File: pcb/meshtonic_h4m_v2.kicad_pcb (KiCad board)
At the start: 6 copper layers, 71.1 x 168.4 mm, 118 parts, among them J1 GROVE-CONNECTOR-DIP_4P-2.0_, J10 Conn_01x02, J11 Conn_01x02, J12 JST_2mm_LiPo, J13 Screw_Terminal_01x02, J14 Micro_SD_Card_passive_clk, J15 H4M_2x6_MDK, J2 GROVE-CONNECTOR-DIP-90D_4P-2.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, J3 GROVE-CONNECTOR-DIP_4P-2.0_, J4 GROVE-CONNECTOR-DIP_4P-2.0_, J5 GROVE-CONNECTOR-DIP_4P-2.0_, J6 GROVE-CONNECTOR-DIP_4P-2.0_, J7 GROVE-CONNECTOR-DIP_4P-2.0_, J8 GROVE-CONNECTOR-SMD_4+2P-2.0_, J9 Conn_01x02, U1 TPS63020DSJR, U2 CN3170, U3 XIAO-S3-Plus, U4 TCA9548APWR, U5 MCP23017x-x-SS

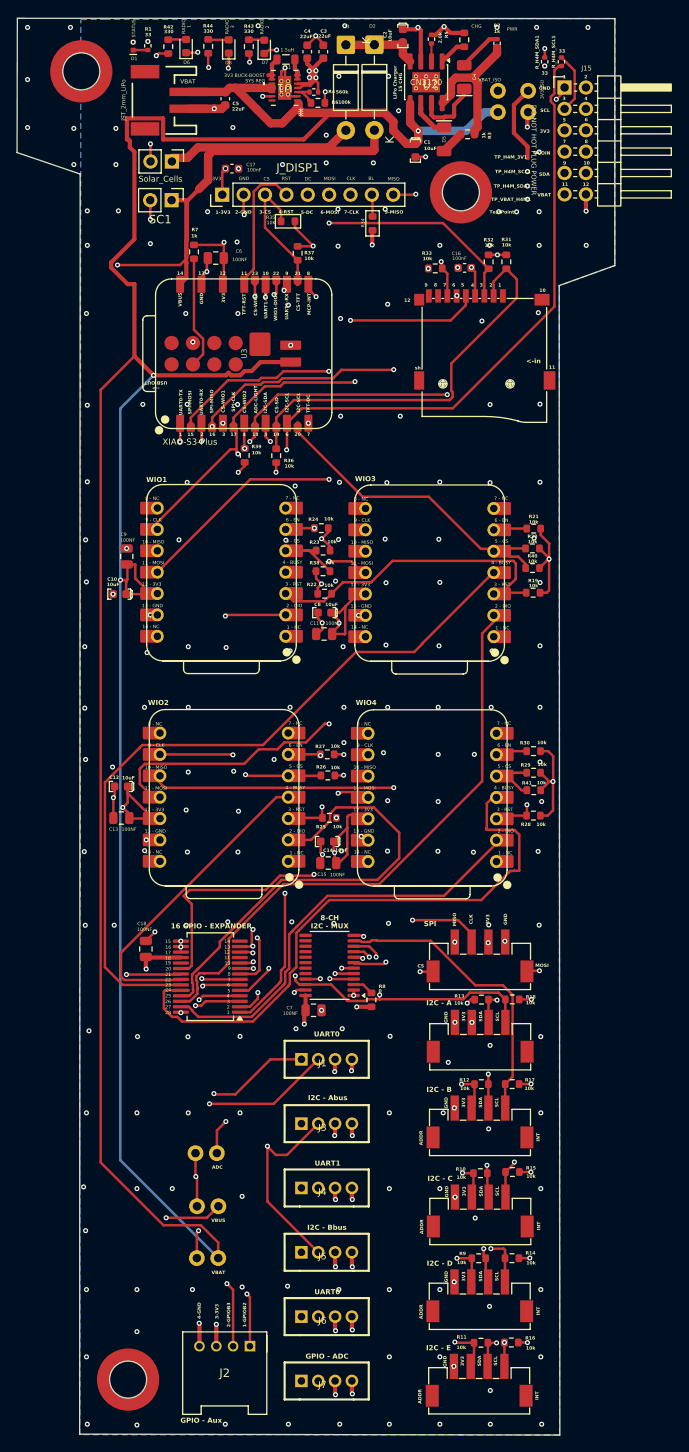
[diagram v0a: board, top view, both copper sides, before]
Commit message: solves no more direct-to-pin vias and routings
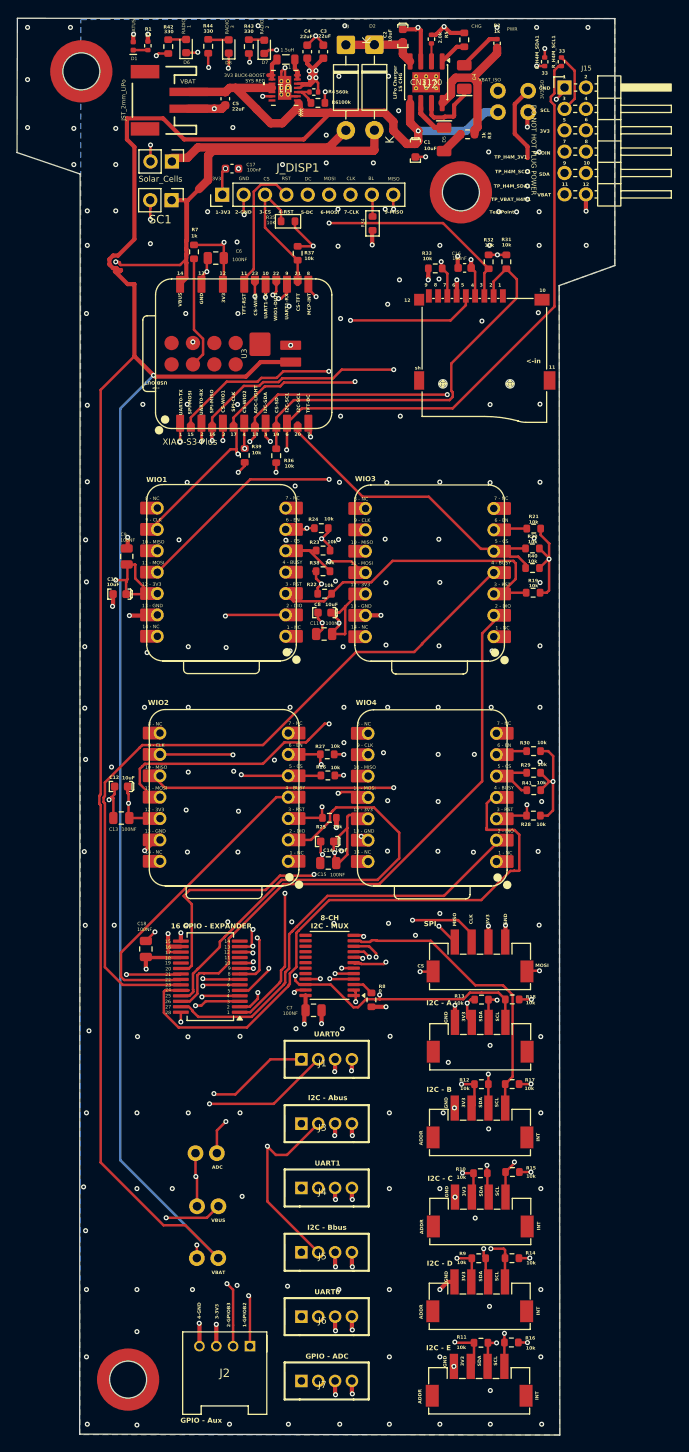
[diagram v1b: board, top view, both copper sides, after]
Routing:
- net GND: track 83.1 -> 108.9 mm, vias 228 -> 230
- net 3V3: track 192.2 -> 198.3 mm, vias 53 -> 52
- net UART1_TX: track 123.2 -> 119.7 mm
- net TFT_DC: track 27.5 -> 31.0 mm
- net SPI_MISO: track 184.0 -> 182.2 mm
- net VBUS: track 201.5 -> 202.9 mm
- net I2C_SDA: track 224.6 -> 223.5 mm
- net VBAT_H4M: track 32.2 -> 31.1 mm
- net WIO4_BUSY: track 71.7 -> 72.5 mm
- net UART0_TX: track 137.2 -> 136.3 mm
- net VBAT: track 378.8 -> 378.0 mm
- net UART0_RX: track 129.6 -> 128.9 mm
- net MCP_GPA7: track 54.2 -> 53.6 mm
- net I2C_SCL: track 223.7 -> 224.4 mm

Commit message: adds licences, top level readme
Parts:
- R34: value R_0603 -> 0
- R35: value R_0603 -> 10k
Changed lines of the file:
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@@
 			)
 		)
-		(property "Datasheet" "https://mm.digikey.com/Volume0/opasdata/d220001/medias/docus/1221/MBKK2012T1R0M_SS.pdf"
+		(property "Datasheet" "https://mm.digikey.com/Volume0/opasdata/d220001/medias/docus/1853/MBKK2012T1R5M_SS.pdf"
 			(at 0 0 180)
 			(unlocked yes)
@@
 			)
 		)
-		(property "Value" "R_0603"
+		(property "Value" "0"
 			(at 0 1.43 90)
 			(layer "F.Fab")
@@
 			)
 		)
-		(property "Value" "R_0603"
+		(property "Value" "10k"
 			(at 0 1.43 0)
 			(layer "F.Fab")
